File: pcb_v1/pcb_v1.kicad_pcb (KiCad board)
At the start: 2 copper layers, 137 parts, among them U1 STM32WB55CGUx

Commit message: Added footprints for LEDs, Rotary Encoder
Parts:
- added LED1: MX_LED_6028R, PCM_marbastlib-mx:LED_MX_6028R, F.Cu at (25.4, 38.1)
- added LED10: MX_LED_6028R, PCM_marbastlib-mx:LED_MX_6028R, F.Cu at (196.8, 38.1)
- added LED11: MX_LED_6028R, PCM_marbastlib-mx:LED_MX_6028R, F.Cu at (215.9, 38.1)
- added LED12: MX_LED_6028R, PCM_marbastlib-mx:LED_MX_6028R, F.Cu at (234.9, 38.1)
- added LED13: MX_LED_6028R, PCM_marbastlib-mx:LED_MX_6028R, F.Cu at (254.0, 38.1)
- added LED14: MX_LED_6028R, PCM_marbastlib-mx:LED_MX_6028R, F.Cu at (282.6, 38.1)
- added LED15: MX_LED_6028R, PCM_marbastlib-mx:LED_MX_6028R, F.Cu at (30.2, 57.1)
- added LED16: MX_LED_6028R, PCM_marbastlib-mx:LED_MX_6028R, F.Cu at (54.0, 57.1)
- added LED17: MX_LED_6028R, PCM_marbastlib-mx:LED_MX_6028R, F.Cu at (73.0, 57.1)
- added LED18: MX_LED_6028R, PCM_marbastlib-mx:LED_MX_6028R, F.Cu at (92.1, 57.1)
- added LED19: MX_LED_6028R, PCM_marbastlib-mx:LED_MX_6028R, F.Cu at (111.1, 57.1)
- added LED2: MX_LED_6028R, PCM_marbastlib-mx:LED_MX_6028R, F.Cu at (44.5, 38.1)
- added LED20: MX_LED_6028R, PCM_marbastlib-mx:LED_MX_6028R, F.Cu at (130.2, 57.1)
- added LED21: MX_LED_6028R, PCM_marbastlib-mx:LED_MX_6028R, F.Cu at (149.2, 57.1)
- added LED22: MX_LED_6028R, PCM_marbastlib-mx:LED_MX_6028R, F.Cu at (168.3, 57.1)
- added LED23: MX_LED_6028R, PCM_marbastlib-mx:LED_MX_6028R, F.Cu at (187.3, 57.1)
- added LED24: MX_LED_6028R, PCM_marbastlib-mx:LED_MX_6028R, F.Cu at (206.4, 57.1)
- added LED25: MX_LED_6028R, PCM_marbastlib-mx:LED_MX_6028R, F.Cu at (225.4, 57.1)
- added LED26: MX_LED_6028R, PCM_marbastlib-mx:LED_MX_6028R, F.Cu at (244.5, 57.1)
- added LED27: MX_LED_6028R, PCM_marbastlib-mx:LED_MX_6028R, F.Cu at (263.5, 57.1)
- added LED28: MX_LED_6028R, PCM_marbastlib-mx:LED_MX_6028R, F.Cu at (287.3, 57.1)
- added LED29: MX_LED_6028R, PCM_marbastlib-mx:LED_MX_6028R, F.Cu at (311.1, 57.1)
- added LED3: MX_LED_6028R, PCM_marbastlib-mx:LED_MX_6028R, F.Cu at (63.5, 38.1)
- added LED30: MX_LED_6028R, PCM_marbastlib-mx:LED_MX_6028R, F.Cu at (32.5, 76.2)
- added LED31: MX_LED_6028R, PCM_marbastlib-mx:LED_MX_6028R, F.Cu at (58.7, 76.2)
- added LED32: MX_LED_6028R, PCM_marbastlib-mx:LED_MX_6028R, F.Cu at (77.8, 76.2)
- added LED33: MX_LED_6028R, PCM_marbastlib-mx:LED_MX_6028R, F.Cu at (96.8, 76.2)
- added LED34: MX_LED_6028R, PCM_marbastlib-mx:LED_MX_6028R, F.Cu at (115.9, 76.2)
- added LED35: MX_LED_6028R, PCM_marbastlib-mx:LED_MX_6028R, F.Cu at (134.9, 76.2)
- added LED36: MX_LED_6028R, PCM_marbastlib-mx:LED_MX_6028R, F.Cu at (154.0, 76.2)
- added LED37: MX_LED_6028R, PCM_marbastlib-mx:LED_MX_6028R, F.Cu at (173.0, 76.2)
- added LED38: MX_LED_6028R, PCM_marbastlib-mx:LED_MX_6028R, F.Cu at (192.1, 76.2)
- added LED39: MX_LED_6028R, PCM_marbastlib-mx:LED_MX_6028R, F.Cu at (211.1, 76.2)
- added LED4: MX_LED_6028R, PCM_marbastlib-mx:LED_MX_6028R, F.Cu at (82.5, 38.1)
- added LED40: MX_LED_6028R, PCM_marbastlib-mx:LED_MX_6028R, F.Cu at (230.2, 76.2)
- added LED41: MX_LED_6028R, PCM_marbastlib-mx:LED_MX_6028R, F.Cu at (249.2, 76.2)
- added LED42: MX_LED_6028R, PCM_marbastlib-mx:LED_MX_6028R, F.Cu at (280.2, 76.2)
- added LED43: MX_LED_6028R, PCM_marbastlib-mx:LED_MX_6028R, F.Cu at (311.1, 76.2)
- added LED44: MX_LED_6028R, PCM_marbastlib-mx:LED_MX_6028R, F.Cu at (37.3, 95.2)
- added LED45: MX_LED_6028R, PCM_marbastlib-mx:LED_MX_6028R, F.Cu at (68.3, 95.2)
- added LED46: MX_LED_6028R, PCM_marbastlib-mx:LED_MX_6028R, F.Cu at (87.3, 95.2)
- added LED47: MX_LED_6028R, PCM_marbastlib-mx:LED_MX_6028R, F.Cu at (106.4, 95.2)
- added LED48: MX_LED_6028R, PCM_marbastlib-mx:LED_MX_6028R, F.Cu at (125.4, 95.2)
- added LED49: MX_LED_6028R, PCM_marbastlib-mx:LED_MX_6028R, F.Cu at (144.5, 95.2)
- added LED5: MX_LED_6028R, PCM_marbastlib-mx:LED_MX_6028R, F.Cu at (101.6, 38.1)
- added LED50: MX_LED_6028R, PCM_marbastlib-mx:LED_MX_6028R, F.Cu at (163.5, 95.2)
- added LED51: MX_LED_6028R, PCM_marbastlib-mx:LED_MX_6028R, F.Cu at (182.6, 95.2)
- added LED52: MX_LED_6028R, PCM_marbastlib-mx:LED_MX_6028R, F.Cu at (201.6, 95.2)
- added LED53: MX_LED_6028R, PCM_marbastlib-mx:LED_MX_6028R, F.Cu at (220.7, 95.2)
- added LED54: MX_LED_6028R, PCM_marbastlib-mx:LED_MX_6028R, F.Cu at (239.7, 95.2)
- added LED55: MX_LED_6028R, PCM_marbastlib-mx:LED_MX_6028R, F.Cu at (265.9, 95.2)
- added LED56: MX_LED_6028R, PCM_marbastlib-mx:LED_MX_6028R, F.Cu at (292.1, 95.2)
- added LED57: MX_LED_6028R, PCM_marbastlib-mx:LED_MX_6028R, F.Cu at (311.1, 95.2)
- added LED58: MX_LED_6028R, PCM_marbastlib-mx:LED_MX_6028R, F.Cu at (28.6, 114.3)
- added LED59: MX_LED_6028R, PCM_marbastlib-mx:LED_MX_6028R, F.Cu at (51.6, 114.3)
- added LED6: MX_LED_6028R, PCM_marbastlib-mx:LED_MX_6028R, F.Cu at (120.7, 38.1)
- added LED60: MX_LED_6028R, PCM_marbastlib-mx:LED_MX_6028R, F.Cu at (75.4, 114.3)
- added LED61: MX_LED_6028R, PCM_marbastlib-mx:LED_MX_6028R, F.Cu at (146.8, 114.2)
- added LED62: MX_LED_6028R, PCM_marbastlib-mx:LED_MX_6028R, F.Cu at (218.3, 114.3)
- added LED63: MX_LED_6028R, PCM_marbastlib-mx:LED_MX_6028R, F.Cu at (242.1, 114.3)
- added LED64: MX_LED_6028R, PCM_marbastlib-mx:LED_MX_6028R, F.Cu at (273.1, 114.3)
- added LED65: MX_LED_6028R, PCM_marbastlib-mx:LED_MX_6028R, F.Cu at (292.1, 114.3)
- added LED66: MX_LED_6028R, PCM_marbastlib-mx:LED_MX_6028R, F.Cu at (311.1, 114.3)
- added LED7: MX_LED_6028R, PCM_marbastlib-mx:LED_MX_6028R, F.Cu at (139.7, 38.1)
- added LED8: MX_LED_6028R, PCM_marbastlib-mx:LED_MX_6028R, F.Cu at (158.8, 38.1)
- added LED9: MX_LED_6028R, PCM_marbastlib-mx:LED_MX_6028R, F.Cu at (177.8, 38.1)
- added SW1: RotaryEncoder, My_Footprints:EN05VS1212NHH, F.Cu at (3.97, 62.4)
- D1, D10, D11, D12, D13, D14, D15, D16, D17, D18, D19, D2, D20, D21, D22, D23, D24, D25, D26, D27, D28, D29, D3, D30, D31, D32, D33, D34, D35, D36, D37, D38, D39, D4, D40, D41, D42, D43, D44, D45, D46, D47, D48, D49, D5, D50, D51, D52, D53, D54, D55, D56, D57, D58, D59, D6, D60, D61, D62, D63, D64, D65, D66, D7, D8, D9, S1, S10, S11, S12, S13, S14, S15, S16, S17, S18, S19, S2, S20, S21, S22, S23, S24, S25, S26, S27, S28, S29, S3, S30, S31, S32, S33, S34, S35, S36, S37, S38, S39, S4, S40, S41, S42, S43, S44, S45, S46, S47, S48, S49, S5, S50, S51, S52, S53, S54, S55, S56, S57, S58, S59, S6, S60, S61, S62, S63, S64, S65, S66, S67, S68, S69, S7, S70, S8, S9, U1: moved to F.Cu
- moved D29 353.3 mm to (-57.9, 38.2), turned to 0 degrees
- moved D43 349.3 mm to (-52.2, 44.9), turned to 0 degrees
- moved D66 347.1 mm to (-40.7, 41.5), turned to 0 degrees
- moved D57 345.8 mm to (-46.4, 51.6), turned to 0 degrees
- moved D28 330.1 mm to (-57.9, 34.8), turned to 0 degrees
- moved D65 329.8 mm to (-40.7, 38.2), turned to 0 degrees
- moved D14 329.7 mm to (-63.7, 28.1), turned to 0 degrees
- moved D56 327.8 mm to (-46.4, 48.2), turned to 0 degrees
- moved D42 319.4 mm to (-52.2, 41.5), turned to 0 degrees
- moved D64 312.7 mm to (-40.7, 34.8), turned to 0 degrees
- moved D27 307.1 mm to (-57.9, 31.5), turned to 0 degrees
- moved D55 303.1 mm to (-46.4, 44.9), turned to 0 degrees
- moved D13 301.6 mm to (-63.7, 24.8), turned to 0 degrees
- moved D41 289.7 mm to (-52.2, 38.2), turned to 0 degrees
- moved D26 288.9 mm to (-57.9, 28.1), turned to 0 degrees
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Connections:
- U1 pad 10: Row2 -> unconnected-(U1-PA1-Pad10)
- U1 pad 11: Row1 -> unconnected-(U1-PA2-Pad11)
- U1 pad 12: Row0 -> unconnected-(U1-PA3-Pad12)
- U1 pad 13: Column0 -> unconnected-(U1-PA4-Pad13)
- U1 pad 14: Column1 -> unconnected-(U1-PA5-Pad14)
- U1 pad 15: Column2 -> unconnected-(U1-PA6-Pad15)
- U1 pad 16: Column3 -> unconnected-(U1-PA7-Pad16)
- U1 pad 17: Column4 -> unconnected-(U1-PA8-Pad17)
- U1 pad 18: Column5 -> unconnected-(U1-PA9-Pad18)
- U1 pad 19: Column6 -> unconnected-(U1-PB2-Pad19)
- U1 pad 28: Column7 -> unconnected-(U1-PB0-Pad28)
- U1 pad 29: Column8 -> unconnected-(U1-PB1-Pad29)
- U1 pad 36: Column9 -> unconnected-(U1-PA10-Pad36)
- U1 pad 37: Column10 -> unconnected-(U1-PA11-Pad37)
- U1 pad 38: Column11 -> unconnected-(U1-PA12-Pad38)
- U1 pad 39: Column12 -> unconnected-(U1-PA13-Pad39)
- U1 pad 41: Column13 -> unconnected-(U1-PA14-Pad41)
- U1 pad 42: Column14 -> unconnected-(U1-PA15-Pad42)
- U1 pad 47: Row4 -> unconnected-(U1-PB7-Pad47)
- U1 pad 9: Row3 -> unconnected-(U1-PA0-Pad9)
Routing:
- net Column14: track 332.7 -> 0.00 mm, vias 3 -> 0
- net Row4: track 332.4 -> 0.00 mm, vias 4 -> 0
- net Column13: track 331.2 -> 0.00 mm, vias 4 -> 0
- net Row3: track 307.6 -> 0.00 mm, vias 2 -> 0
- net Column11: track 299.3 -> 0.00 mm, vias 3 -> 0
- net Row2: track 292.7 -> 0.00 mm
- net Row1: track 288.4 -> 0.00 mm
- net Row0: track 282.5 -> 0.00 mm, vias 2 -> 0
- net Column12: track 275.0 -> 0.00 mm, vias 3 -> 0
- net Column10: track 272.8 -> 0.00 mm, vias 3 -> 0
- net Column9: track 241.0 -> 0.00 mm, vias 1 -> 0
- net Column8: track 201.2 -> 0.00 mm, vias 1 -> 0
- net Column7: track 182.2 -> 0.00 mm, vias 1 -> 0
- net Column5: track 170.7 -> 0.00 mm, vias 1 -> 0
- net Column6: track 169.2 -> 0.00 mm, vias 1 -> 0
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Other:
- board outline added: 5.8 x 2.9 mm

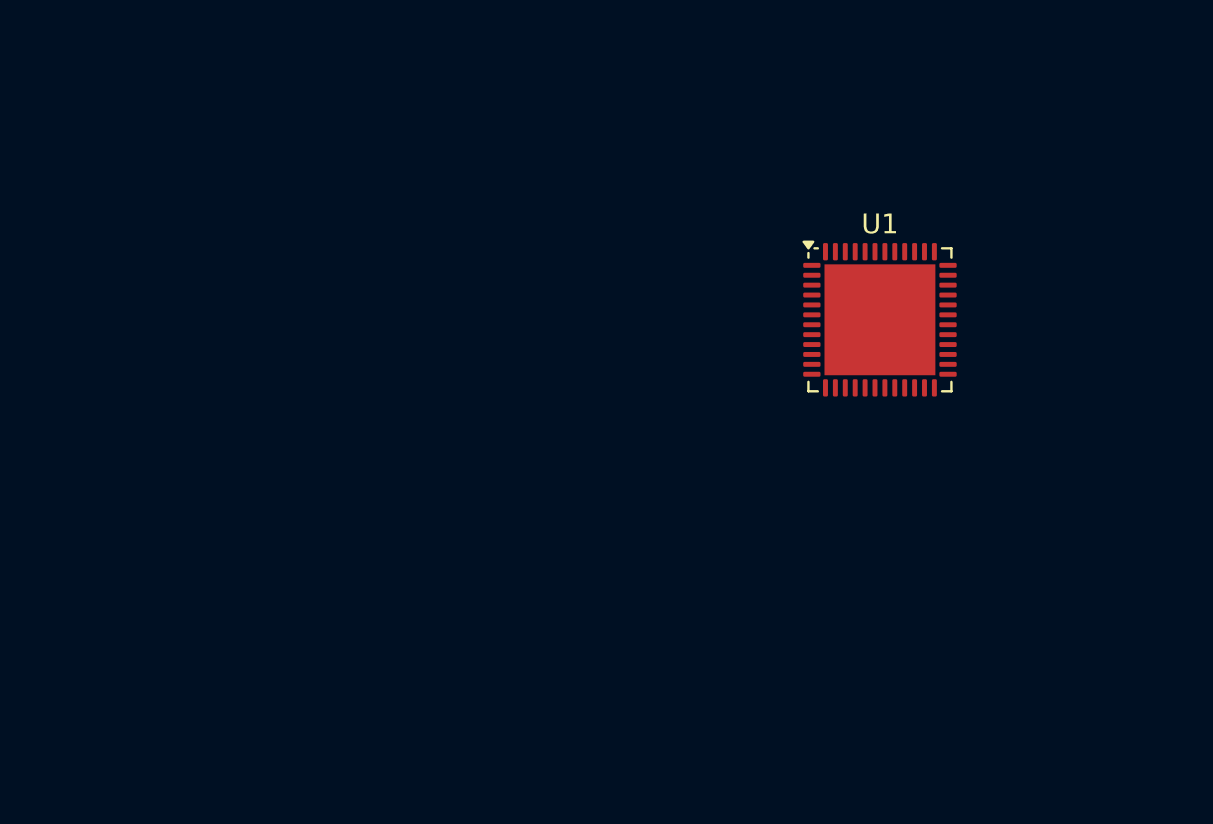
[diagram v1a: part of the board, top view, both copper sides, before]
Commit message: Included Capacitors and JST connector in schematic. Upgraded MC to 69 pin version
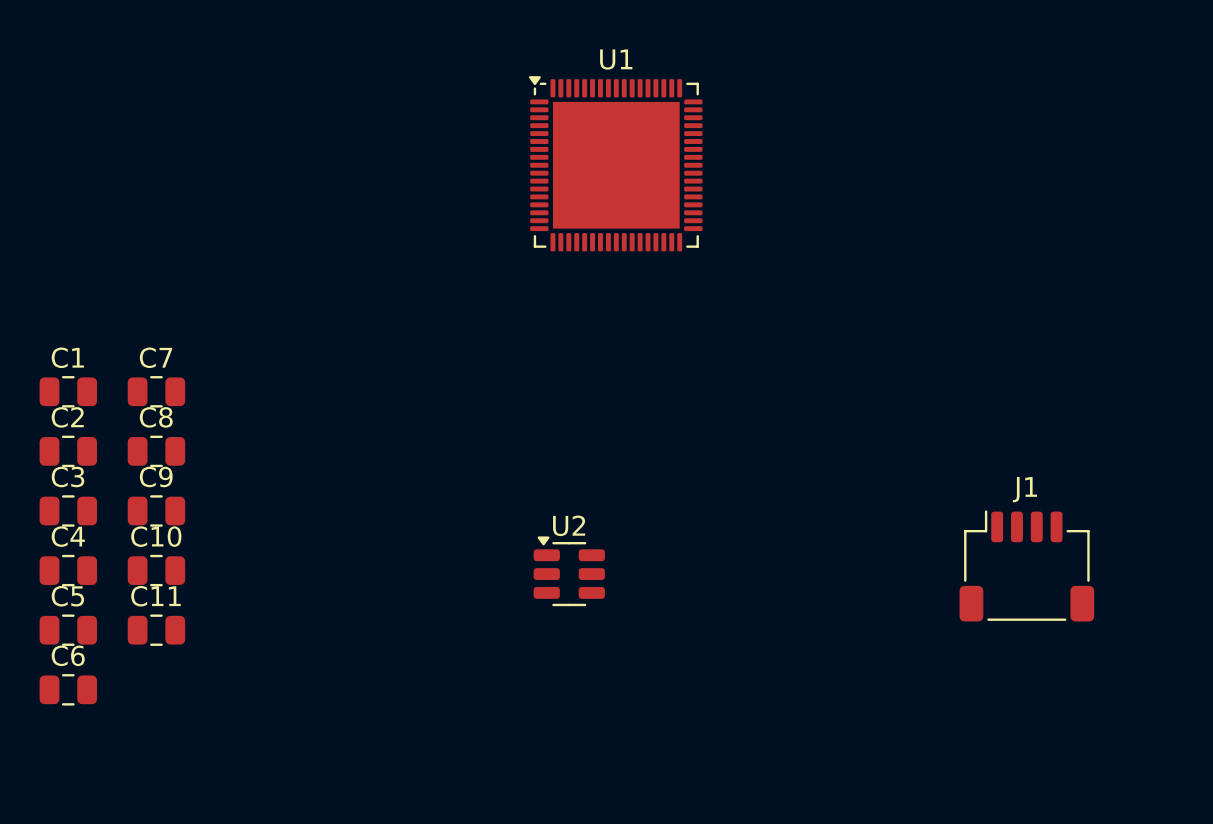
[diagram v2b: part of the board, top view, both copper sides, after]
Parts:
- added C1: 100nF, Capacitor_SMD:C_0805_2012Metric, F.Cu at (-72.1, -9.21)
- added C10: 4.7uF, Capacitor_SMD:C_0805_2012Metric, F.Cu at (-67.7, -0.17)
- added C11: 100nF, Capacitor_SMD:C_0805_2012Metric, F.Cu at (-67.7, 2.83)
- added C2: 100nF, Capacitor_SMD:C_0805_2012Metric, F.Cu at (-72.1, -6.20)
- added C3: 100nF, Capacitor_SMD:C_0805_2012Metric, F.Cu at (-72.1, -3.19)
- added C4: 100nF, Capacitor_SMD:C_0805_2012Metric, F.Cu at (-72.1, -0.17)
- added C5: 100nF, Capacitor_SMD:C_0805_2012Metric, F.Cu at (-72.1, 2.83)
- added C6: 100nF, Capacitor_SMD:C_0805_2012Metric, F.Cu at (-72.1, 5.84)
- added C7: 100nF, Capacitor_SMD:C_0805_2012Metric, F.Cu at (-67.7, -9.21)
- added C8: 100nF, Capacitor_SMD:C_0805_2012Metric, F.Cu at (-67.7, -6.20)
- added C9: 10nF, Capacitor_SMD:C_0805_2012Metric, F.Cu at (-67.7, -3.19)
- added J1: Conn_01x04, Connector_JST:JST_SH_SM04B-SRSS-TB_1x04-1MP_P1.00mm_Horizontal, F.Cu at (-23.7, -0.38)
- added U2: SRV05-4, Package_TO_SOT_SMD:SOT-23-6, F.Cu at (-46.8, 0.00)
- U1: value STM32WB55CGUx -> STM32WB55RGVx; footprint Package_DFN_QFN:QFN-48-1EP_7x7mm_P0.5mm_EP5.6x5.6mm -> Package_DFN_QFN:QFN-68-1EP_8x8mm_P0.4mm_EP6.4x6.4mm
- moved U1 15.4 mm to (-44.5, -20.6)
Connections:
- LED1 pad 2: PWRG -> PWRR
- LED10 pad 2: PWRG -> PWRR
- LED11 pad 2: PWRG -> PWRR
- LED12 pad 2: PWRG -> PWRR
- LED13 pad 2: PWRG -> PWRR
- LED14 pad 2: PWRG -> PWRR
- LED15 pad 2: PWRG -> PWRR
- LED16 pad 2: unconnected-(LED16-RK-Pad2) -> PWRR
- LED17 pad 2: PWRG -> PWRR
- LED18 pad 2: PWRG -> PWRR
- LED19 pad 2: PWRG -> PWRR
- LED2 pad 2: PWRG -> PWRR
- LED20 pad 2: PWRG -> PWRR
- LED21 pad 1: unconnected-(LED21-GK-Pad1) -> PWRG
- LED21 pad 2: PWRG -> PWRR
- LED22 pad 1: unconnected-(LED22-GK-Pad1) -> PWRG
- LED22 pad 2: PWRG -> PWRR
- LED23 pad 2: PWRG -> PWRR
- LED24 pad 2: PWRG -> PWRR
- LED25 pad 2: PWRG -> PWRR
- LED26 pad 2: PWRG -> PWRR
- LED27 pad 2: PWRG -> PWRR
- LED28 pad 2: PWRG -> PWRR
- LED29 pad 2: PWRG -> PWRR
- LED3 pad 2: unconnected-(LED3-RK-Pad2) -> PWRR
- LED30 pad 2: PWRG -> PWRR
- LED31 pad 2: PWRG -> PWRR
- LED32 pad 2: PWRG -> PWRR
- LED33 pad 2: PWRG -> PWRR
- LED34 pad 2: PWRG -> PWRR
- LED35 pad 2: PWRG -> PWRR
- LED36 pad 2: PWRG -> PWRR
- LED37 pad 2: PWRG -> PWRR
- LED38 pad 2: PWRG -> PWRR
- LED39 pad 2: PWRG -> PWRR
- LED4 pad 2: unconnected-(LED4-RK-Pad2) -> PWRR
- LED40 pad 2: PWRG -> PWRR
- LED41 pad 2: PWRG -> PWRR
- LED42 pad 2: PWRG -> PWRR
- LED43 pad 2: PWRG -> PWRR
- LED44 pad 2: PWRG -> PWRR
- LED45 pad 2: PWRG -> PWRR
- LED46 pad 2: PWRG -> PWRR
- LED47 pad 2: PWRG -> PWRR
- LED48 pad 2: PWRG -> PWRR
- LED49 pad 2: PWRG -> PWRR
- LED5 pad 2: PWRG -> PWRR
- LED50 pad 2: PWRG -> PWRR
- LED51 pad 2: PWRG -> PWRR
- LED52 pad 2: PWRG -> PWRR
- LED53 pad 2: PWRG -> PWRR
- LED54 pad 2: PWRG -> PWRR
- LED55 pad 2: PWRG -> PWRR
- LED56 pad 2: PWRG -> PWRR
- LED57 pad 2: PWRG -> PWRR
- LED58 pad 2: PWRG -> PWRR
- LED59 pad 2: PWRG -> PWRR
- LED6 pad 2: PWRG -> PWRR
- LED60 pad 2: PWRG -> PWRR
- LED61 pad 2: unconnected-(LED61-RK-Pad2) -> PWRR
- LED62 pad 2: PWRG -> PWRR
- LED64 pad 2: PWRG -> PWRR
- LED65 pad 2: PWRG -> PWRR
- LED66 pad 2: PWRG -> PWRR
- LED7 pad 2: PWRG -> PWRR
- LED8 pad 2: PWRG -> PWRR
- LED9 pad 2: PWRG -> PWRR
- U1 pad 1: unconnected-(U1-VBAT-Pad1) -> +3.3V
- U1 pad 14: unconnected-(U1-PA5-Pad14) -> +3.3V
- U1 pad 30: unconnected-(U1-PE4-Pad30) -> +3.3V
- U1 pad 32: unconnected-(U1-VSSSMPS-Pad32) -> GND
- U1 pad 33: unconnected-(U1-VLXSMPS-Pad33) -> +3.3V
- U1 pad 42: unconnected-(U1-PA15-Pad42) -> GND
- U1 pad 44: unconnected-(U1-PB4-Pad44) -> +3.3V
- U1 pad 45: unconnected-(U1-PB5-Pad45) -> +3.3V

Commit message: Added Flex Cuts
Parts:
- added BT1: LIPO, Connector_PinHeader_2.54mm:PinHeader_1x02_P2.54mm_Vertical_SMD_Pin1Left, F.Cu at (8.66, -84.6)
- added C12: 100nF, Capacitor_SMD:C_0805_2012Metric, F.Cu at (-47.4, -53.3)
- added C13: 1uF, Capacitor_SMD:C_0805_2012Metric, F.Cu at (-47.4, -50.2)
- added C14: 1uF, Capacitor_SMD:C_0805_2012Metric, F.Cu at (-47.4, -47.2)
- added C15: 0.1uF, Capacitor_SMD:C_0603_1608Metric, F.Cu at (2.72, -96.3)
- added C16: 0.1uF, Capacitor_SMD:C_0603_1608Metric, F.Cu at (2.72, -93.7)
- added C17: 4,7uF, Capacitor_SMD:C_0603_1608Metric, F.Cu at (2.72, -91.2)
- added D67: LED, LED_SMD:LED_0603_1608Metric, F.Cu at (10.7, -110.5)
- added H1: MountingHole_Pad, MountingHole:MountingHole_3.2mm_M3_DIN965_Pad, F.Cu at (-14.4, -108.2)
- added H2: MountingHole_Pad, MountingHole:MountingHole_3.2mm_M3_DIN965_Pad, F.Cu at (-14.4, -101.1)
- added H3: MountingHole_Pad, MountingHole:MountingHole_3.2mm_M3_DIN965_Pad, F.Cu at (-7.21, -108.2)
- added H4: MountingHole_Pad, MountingHole:MountingHole_3.2mm_M3_DIN965_Pad, F.Cu at (-7.21, -101.1)
- added H5: MountingHole_Pad, MountingHole:MountingHole_3.2mm_M3_DIN965_Pad, F.Cu at (-0.06, -108.2)
- added H6: MountingHole_Pad, MountingHole:MountingHole_3.2mm_M3_DIN965_Pad, F.Cu at (-0.06, -101.1)
- added J2: power Switch, Connector_PinHeader_2.54mm:PinHeader_1x03_P2.54mm_Vertical_SMD_Pin1Left, F.Cu at (-4.15, -85.0)
- added J5: 10x1mm FFC/FPC, Connector_FFC-FPC:Molex_200528-0100_1x10-1MP_P1.00mm_Horizontal, F.Cu at (-8.61, -95.1)
- added M1: DMG6968U-7_single, Package_TO_SOT_SMD:TSOT-23, F.Cu at (7.42, -95.1)
- added M2: DMG6968U-7_single, Package_TO_SOT_SMD:TSOT-23, F.Cu at (7.42, -90.4)
- added Q1: DMG6968UMD, Package_TO_SOT_SMD:SOT-23-6_Handsoldering, F.Cu at (6.44, -100.1)
- added R2: 330, Resistor_SMD:R_0603_1608Metric, F.Cu at (2.72, -88.7)
- added R3: 2k7, Resistor_SMD:R_0603_1608Metric, F.Cu at (2.72, -86.2)
- added R4: 10k/2k, Resistor_SMD:R_0603_1608Metric, F.Cu at (2.72, -83.7)
- added R5: 150, Resistor_SMD:R_0603_1608Metric, F.Cu at (2.72, -81.2)
- added U3: XC6206PxxxMR, Package_TO_SOT_SMD:SOT-23-3, F.Cu at (-42.6, -48.1)
- added U4: MCP1825S, Package_TO_SOT_SMD:SOT-223-3_TabPin2, F.Cu at (-13.0, -85.7)
- added U5: AP9101CK, Package_TO_SOT_SMD:SOT-23-5, F.Cu at (6.09, -109.4)
- added U6: MCP73831-2-OT, Package_TO_SOT_SMD:SOT-23-5, F.Cu at (6.09, -104.8)
- moved J1 91.0 mm to (-50.7, -87.4)
- moved C1 91.0 mm to (-99.1, -96.2)
- moved C10 91.0 mm to (-94.6, -87.1)
- moved C11 91.0 mm to (-94.6, -84.1)
- moved C2 91.0 mm to (-99.1, -93.2)
- moved C3 91.0 mm to (-99.1, -90.2)
- moved C4 91.0 mm to (-99.1, -87.1)
- moved C5 91.0 mm to (-99.1, -84.1)
- moved C6 91.0 mm to (-99.1, -81.1)
- moved C7 91.0 mm to (-94.6, -96.2)
- moved C8 91.0 mm to (-94.6, -93.2)
- moved C9 91.0 mm to (-94.6, -90.2)
- moved D1 91.0 mm to (-96.4, -62.2)
- moved D10 91.0 mm to (-96.4, -32.1)
- moved D11 91.0 mm to (-96.4, -28.7)
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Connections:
- U1 pad 5: unconnected-(U1-PH3-Pad5) -> BOOT0
- U1 pad 8: unconnected-(U1-NRST-Pad8) -> Net-(U1-NRST)
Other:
- board size 5.8 x 2.9 mm -> 320.7 x 96.8 mm

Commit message: Re-drew PCB. Flipped to the correct orientation
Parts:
- removed BT1: LIPO, Connector_PinHeader_2.54mm:PinHeader_1x02_P2.54mm_Vertical_SMD_Pin1Left
- removed C13, C14: 1uF, Capacitor_SMD:C_0805_2012Metric
- removed H1, H2, H3, H4, H5, H6: MountingHole_Pad, MountingHole:MountingHole_3.2mm_M3_DIN965_Pad
- removed J2: power Switch, Connector_PinHeader_2.54mm:PinHeader_1x03_P2.54mm_Vertical_SMD_Pin1Left
- removed J5: 10x1mm FFC/FPC, Connector_FFC-FPC:Molex_200528-0100_1x10-1MP_P1.00mm_Horizontal
- removed M1, M2: DMG6968U-7_single, Package_TO_SOT_SMD:TSOT-23
- removed Q1: DMG6968UMD, Package_TO_SOT_SMD:SOT-23-6_Handsoldering
- removed R5: 150, Resistor_SMD:R_0603_1608Metric
- removed U3: XC6206PxxxMR, Package_TO_SOT_SMD:SOT-23-3
- removed U6: MCP73831-2-OT, Package_TO_SOT_SMD:SOT-23-5
- added C18: 1uF, Capacitor_SMD:C_0805_2012Metric, B.Cu at (-280.4, -167.0)
- added C19: 1uF, Capacitor_SMD:C_0805_2012Metric, B.Cu at (-280.4, -163.9)
- added D68: B5819W SL, Diode_SMD:D_SOD-123, B.Cu at (-279.0, -154.4)
- added P2: BATT, Connector_PinHeader_2.54mm:PinHeader_1x02_P2.54mm_Vertical, B.Cu at (-284.9, -155.7)
- added P3: BATT, Connector_PinSocket_2.00mm:PinSocket_1x02_P2.00mm_Vertical, B.Cu at (-294.2, -165.2)
- C1, C10, C11, C12, C2, C3, C4, C5, C6, C7, C8, C9, D1, D10, D11, D12, D13, D14, D15, D16, D17, D18, D19, D2, D20, D21, D22, D23, D24, D25, D26, D27, D28, D29, D3, D30, D31, D32, D33, D34, D35, D36, D37, D38, D39, D4, D40, D41, D42, D43, D44, D45, D46, D47, D48, D49, D5, D50, D51, D52, D53, D54, D55, D56, D57, D58, D59, D6, D60, D61, D62, D63, D64, D65, D66, D7, D8, D9, J1, LED1, LED10, LED11, LED12, LED13, LED14, LED15, LED16, LED17, LED18, LED19, LED2, LED20, LED21, LED22, LED23, LED24, LED25, LED26, LED27, LED28, LED29, LED3, LED30, LED31, LED32, LED33, LED34, LED35, LED36, LED37, LED38, LED39, LED4, LED40, LED41, LED42, LED43, LED44, LED45, LED46, LED47, LED48, LED49, LED5, LED50, LED51, LED52, LED53, LED54, LED55, LED56, LED57, LED58, LED59, LED6, LED60, LED61, LED62, LED63, LED64, LED65, LED66, LED7, LED8, LED9, S1, S10, S11, S12, S13, S14, S15, S16, S17, S18, S19, S2, S20, S21, S22, S23, S24, S25, S26, S27, S28, S29, S3, S30, S31, S32, S33, S34, S35, S36, S37, S38, S39, S4, S40, S41, S42, S43, S44, S45, S46, S47, S48, S49, S5, S50, S51, S52, S53, S54, S55, S56, S57, S58, S59, S6, S60, S61, S62, S63, S64, S65, S66, S67, S68, S69, S7, S70, S8, S9, SW1, U1, U2: moved to B.Cu
- C15: footprint Capacitor_SMD:C_0603_1608Metric -> Capacitor_SMD:C_0805_2012Metric; moved to B.Cu
- C16: value 0.1uF -> 10nF; footprint Capacitor_SMD:C_0603_1608Metric -> Capacitor_SMD:C_0805_2012Metric; moved to B.Cu
- C17: value 4,7uF -> 1uF; footprint Capacitor_SMD:C_0603_1608Metric -> Capacitor_SMD:C_0805_2012Metric; moved to B.Cu
- D67: value LED -> B5819W SL; footprint LED_SMD:LED_0603_1608Metric -> Diode_SMD:D_SOD-123; moved to B.Cu
- R2: value 330 -> 4.7K; footprint Resistor_SMD:R_0603_1608Metric -> Resistor_SMD:R_0805_2012Metric; moved to B.Cu
- R3: value 2k7 -> 10M; footprint Resistor_SMD:R_0603_1608Metric -> Resistor_SMD:R_0805_2012Metric; moved to B.Cu
- R4: value 10k/2k -> 2.2M; footprint Resistor_SMD:R_0603_1608Metric -> Resistor_SMD:R_0805_2012Metric; moved to B.Cu
- U4: value MCP1825S -> TP4057; footprint Package_TO_SOT_SMD:SOT-223-3_TabPin2 -> Package_TO_SOT_SMD:SOT-23-6; moved to B.Cu
- U5: value AP9101CK -> XC6206P33; footprint Package_TO_SOT_SMD:SOT-23-5 -> Package_TO_SOT_SMD:SOT-23; moved to B.Cu
- moved R2 302.7 mm to (-290.0, -165.7), turned to 180 degrees
- moved R3 302.6 mm to (-290.0, -162.8), turned to 180 degrees
- moved R4 302.5 mm to (-290.0, -159.8), turned to 180 degrees
- moved C15 294.2 mm to (-280.4, -176.0), turned to 180 degrees
- moved C16 294.0 mm to (-280.4, -173.0), turned to 180 degrees
- moved C17 293.9 mm to (-280.4, -170.0), turned to 180 degrees
- moved D67 293.6 mm to (-279.0, -157.8), turned to 180 degrees
- moved LED58 282.7 mm to (-73.8, -149.2), turned to 180 degrees
- moved LED15 282.6 mm to (-71.8, -206.4), turned to 180 degrees
- moved LED1 282.4 mm to (-76.2, -225.4), turned to 180 degrees
- moved LED10 282.4 mm to (95.2, -225.4), turned to 180 degrees
- moved LED11 282.4 mm to (114.3, -225.4), turned to 180 degrees
- moved LED12 282.4 mm to (133.3, -225.4), turned to 180 degrees
- moved LED13 282.4 mm to (152.4, -225.4), turned to 180 degrees
- moved LED14 282.4 mm to (181.0, -225.4), turned to 180 degrees
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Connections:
- C15 pad 1: +3V3 -> VCC
- C16 pad 1: Net-(U5-VDD) -> ADC1
- C16 pad 2: /Battery Recharge/bat- -> GND
- C17 pad 1: /Battery Recharge/VBUS -> BATT
- D67 pad 2: /Battery Recharge/VBUS -> VCC
- R2 pad 1: Net-(U5-VDD) -> Net-(U4-PROG)
- R2 pad 2: Net-(BT1-+) -> GND
- R3 pad 1: Net-(U5-VM) -> BATT
- R3 pad 2: GND -> ADC1
- R4 pad 1: GND -> ADC1
- R4 pad 2: Net-(U6-PROG) -> GND
- U4 pad 1: HV_CHR -> CHRG
- U4 pad 3: +3V3 -> BATT
- U5 pad 1: Net-(U5-VM) -> GND
- U5 pad 2: Net-(U5-VDD) -> 3V3
- U5 pad 3: /Battery Recharge/bat- -> Net-(D67-K)
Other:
- board size 320.7 x 96.8 mm -> 325.4 x 97.6 mm

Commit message: Basic Routing around flex cuts
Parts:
- moved D13 403.6 mm to (160.8, -231.4), turned to 90 degrees
- moved D12 383.8 mm to (141.6, -231.4), turned to 90 degrees
- moved D11 364.5 mm to (122.6, -231.4), turned to 90 degrees
- moved D10 345.2 mm to (103.6, -231.4), turned to 90 degrees
- moved D9 325.7 mm to (84.4, -231.4), turned to 90 degrees
- moved D8 306.4 mm to (65.4, -231.2), turned to 90 degrees
- moved D7 287.1 mm to (46.4, -231.4), turned to 90 degrees
- moved D6 267.8 mm to (27.4, -231.2), turned to 90 degrees
- moved D5 248.5 mm to (8.40, -231.4), turned to 90 degrees
- moved D4 229.1 mm to (-10.8, -231.4), turned to 90 degrees
- moved D3 209.8 mm to (-29.8, -231.4), turned to 90 degrees
- moved D2 190.5 mm to (-48.8, -231.6), turned to 90 degrees
- moved U1 188.7 mm to (-246.8, -183.3)
- moved D1 171.2 mm to (-67.8, -231.6), turned to 90 degrees
- moved D16 143.4 mm to (-117.4, -259.9)
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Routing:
- net Column5: track 0.00 -> 797.7 mm, vias 0 -> 7
- net Column7: track 0.00 -> 612.1 mm, vias 0 -> 5
- net Column8: track 0.00 -> 547.3 mm, vias 0 -> 5
- net Column6: track 0.00 -> 520.8 mm, vias 0 -> 5
- net Column9: track 0.00 -> 469.2 mm, vias 0 -> 7
- net Column10: track 0.00 -> 395.7 mm, vias 0 -> 7
- net Column3: track 0.00 -> 327.8 mm, vias 0 -> 5
- net Column4: track 0.00 -> 291.5 mm, vias 0 -> 5
- net Row0: track 0.00 -> 273.3 mm
- net Net-(D6-A): track 0.00 -> 6.81 mm
- net Net-(D13-A): track 0.00 -> 6.78 mm
- net Net-(D5-A): track 0.00 -> 6.78 mm
- net Net-(D10-A): track 0.00 -> 6.73 mm
- net Net-(D3-A): track 0.00 -> 6.68 mm
- net Net-(D7-A): track 0.00 -> 6.68 mm
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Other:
- outline, holes or cut-outs redrawn
